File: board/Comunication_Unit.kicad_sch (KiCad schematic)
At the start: 1 part, among them U2 MAX485E

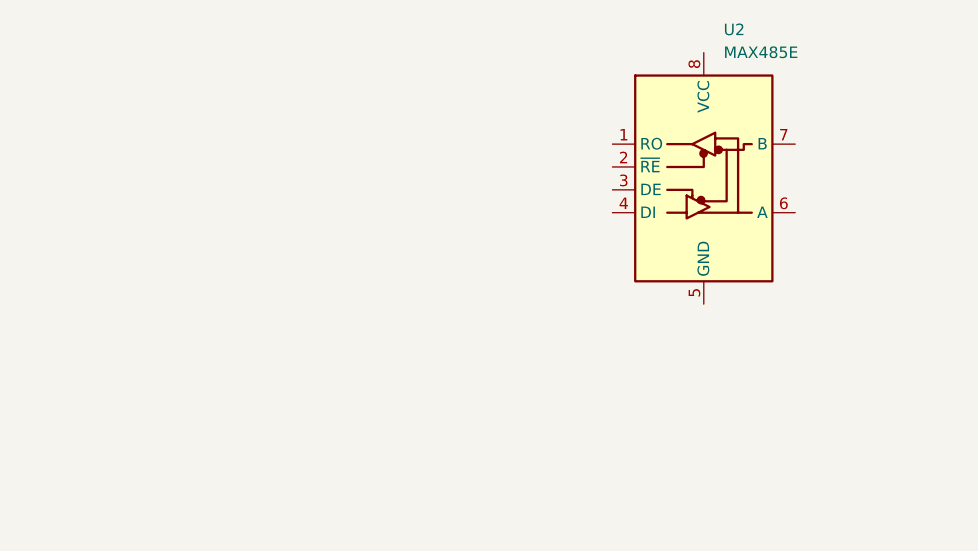
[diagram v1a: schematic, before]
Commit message: [23-5-2024] add RS485 and CAN Appnote/Datasheet
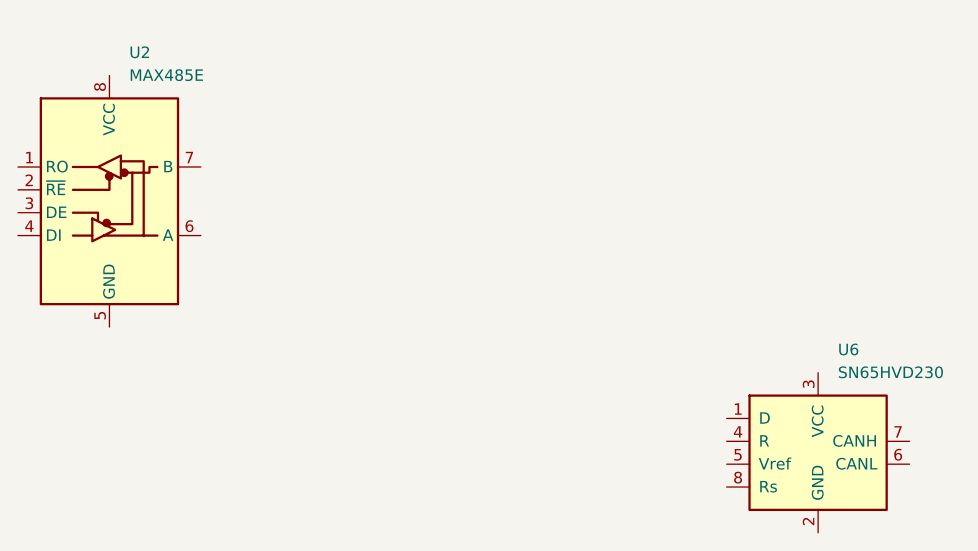
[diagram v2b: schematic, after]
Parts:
- added U6: SN65HVD230, Package_SO:SOIC-8_3.9x4.9mm_P1.27mm, symbol Interface_CAN_LIN:SN65HVD230
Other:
- moved on the sheet: U2
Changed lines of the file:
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@@
 	(paper "A4")
 	(symbol
+		(lib_id "Interface_CAN_LIN:SN65HVD230")
+		(at 146.05 132.08 0)
+		(unit 1)
+		(exclude_from_sim no)
+		(in_bom yes)
+		(on_board yes)
+		(dnp no)
+		(fields_autoplaced yes)
+		(property "Reference" "U6"
+			(at 148.2441 121.92 0)
+			(effects
+				(font
+					(size 1.27 1.27)
+				)
+				(justify left)
+			)
+		)
+		(property "Value" "SN65HVD230"
+			(at 148.2441 124.46 0)
+			(effects
+				(font
+					(size 1.27 1.27)
+				)
+				(justify left)
+			)
+		)
+		(property "Footprint" "Package_SO:SOIC-8_3.9x4.9mm_P1.27mm"
+			(at 146.05 144.78 0)
+			(effects
+				(font
+					(size 1.27 1.27)
+				)
+				(hide yes)
+			)
+		)
+		(property "Datasheet" "http://www.ti.com/lit/ds/symlink/sn65hvd230.pdf"
+			(at 143.51 121.92 0)
+			(effects
+				(font
+					(size 1.27 1.27)
+				)
+				(hide yes)
+			)
+		)
+		(property "Description" "CAN Bus Transceivers, 3.3V, 1Mbps, Low-Power capabilities, SOIC-8"
+			(at 146.05 132.08 0)
+			(effects
+				(font
+					(size 1.27 1.27)
+				)
+				(hide yes)
+			)
+		)
+		(pin "5"
+		)
+		(pin "1"
+		)
+		(pin "8"
+		)
+		(pin "6"
+		)
+		(pin "7"
+		)
+		(pin "2"
+		)
+		(pin "4"
+		)
+		(pin "3"
+		)
+		(instances
+			(project "clsm"
+				(path "/508e0e3b-a744-4e88-93ea-e872e80e580c/05a8634a-0690-42f6-ae5c-b11bdb587ff8"
+					(reference "U6")
+					(unit 1)
+				)
+			)
+		)
+	)
+	(symbol
 		(lib_id "Interface_UART:MAX485E")
-		(at 133.35 101.6 0)
+		(at 67.31 104.14 0)
 		(unit 1)
 		(exclude_from_sim yes)
@@
 		(dnp no)
 		(property "Reference" "U2"
-			(at 135.5441 86.36 0)
+			(at 69.5041 88.9 0)
 			(effects
 				(font
@@
 		)
 		(property "Value" "MAX485E"
-			(at 135.5441 88.9 0)
+			(at 69.5041 91.44 0)
 			(effects
 				(font
@@
 		)
 		(property "Footprint" ""
-			(at 133.35 119.38 0)
+			(at 67.31 121.92 0)
 			(effects
 				(font
@@
 		)
 		(property "Datasheet" "https://datasheets.maximintegrated.com/en/ds/MAX1487E-MAX491E.pdf"
-			(at 133.35 100.33 0)
+			(at 67.31 102.87 0)
 			(effects
 				(font
@@
 		)
 		(property "Description" "Half duplex RS-485/RS-422, 2.5 Mbps, ±15kV electro-static discharge (ESD) protection, no slew-rate, no low-power shutdown, with receiver/driver enable, 32 receiver drive capability, DIP-8 and SOIC-8"
-			(at 133.35 101.6 0)
+			(at 67.31 104.14 0)
 			(effects
 				(font
